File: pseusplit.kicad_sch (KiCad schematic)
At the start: 146 parts, among them J1 USB_C_Receptacle_USB2.0_14P, J3 ST7789 320x240, Q1 DTC123J, SW1 Reset_SW, U1 IS31FL3733-QF, U2 XC6206PxxxMR, U4 STM32G0B1CBTx, U5 SRV05-4

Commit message: Update some part numbers, remove unnecessary MPN symbol field, dos2unix CSV files
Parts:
- C1, C2, C4, C6: MPN C13967 -> (none)
- C10, C11: MPN C28323 -> (none)
- C12, C9: MPN C1744 -> (none)
- C13: MPN C15850 -> (none)
- C14, C16: MPN C28233 -> (none)
- C17, C18: MPN C1779 -> (none)
- C3, C5, C7: MPN C49678 -> (none)
- C8: MPN C45783 -> (none)
- D1, D10, D11, D12, D13, D14, D15, D16, D17, D18, D19, D2, D20, D21, D22, D23, D24, D25, D26, D27, D28, D29, D3, D30, D31, D32, D33, D34, D37, D38, D39, D4, D5, D6, D7, D8, D9: MPN C81598 -> (none)
- D40: MPN C2297 -> (none)
- F1: MPN C2830238 -> (none)
- J1: MPN C165948 -> (none)
- LED1, LED10, LED11, LED12, LED13, LED14, LED15, LED16, LED17, LED18, LED19, LED2, LED20, LED21, LED22, LED23, LED24, LED25, LED26, LED27, LED28, LED29, LED3, LED30, LED31, LED32, LED33, LED34, LED35, LED36, LED4, LED5, LED6, LED7, LED8, LED9: MPN C183826 -> (none)
- Q1: MPN C20616358 -> (none)
- R1: MPN C4328 -> (none)
- R11, R2: MPN C149504 -> (none)
- R12, R7, R8: MPN C27834 -> (none)
- R3: MPN C17414 -> (none)
- R4, R5: MPN C17604 -> (none)
- R6: MPN C17514 -> (none)
- SW1: MPN C318884 -> (none)
- U1: MPN C506251 -> (none)
- U2: MPN C5446 -> (none)
- U4: MPN C2847904 -> (none)
- U5: MPN C558418 -> (none)

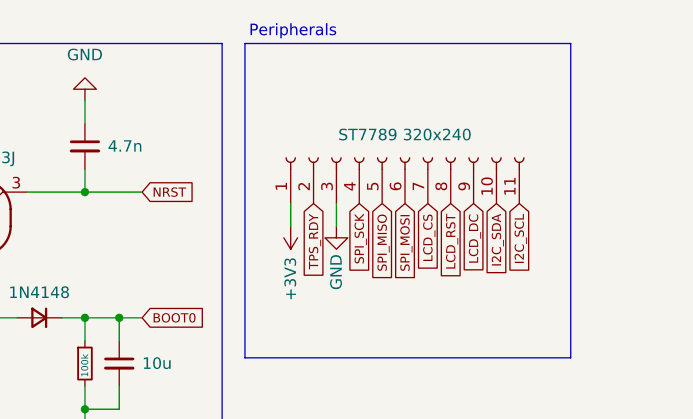
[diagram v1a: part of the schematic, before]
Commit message: Update tantalum capacitor footprint & part, remove LEDs from BOM & provide link
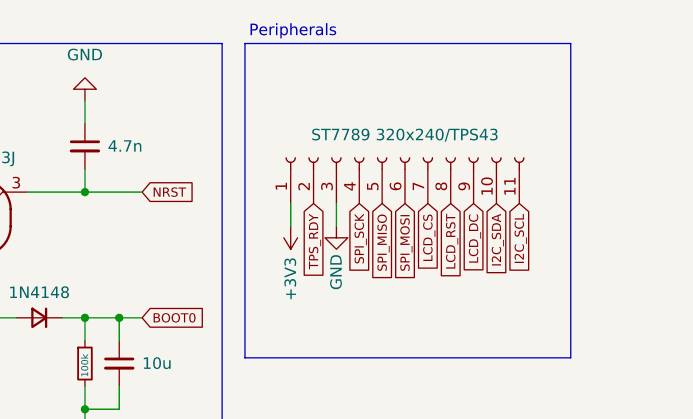
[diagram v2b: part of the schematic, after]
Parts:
- C8: footprint Capacitor_SMD:C_0805_2012Metric -> Capacitor_Tantalum_SMD:CP_EIA-3216-18_Kemet-A
- J3: value ST7789 320x240 -> ST7789 320x240/TPS43
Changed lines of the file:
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@@
 	(title_block
 		(title "pseusplit keyboard")
-		(date "2025-06-08")
+		(date "2025-06-25")
 		(rev "0.1.0")
 		(company "jack@pngu.org")
@@
 			)
 		)
-		(property "Footprint" "Capacitor_SMD:C_0805_2012Metric"
+		(property "Footprint" "Capacitor_Tantalum_SMD:CP_EIA-3216-18_Kemet-A"
 			(at 246.38 111.76 0)
 			(effects
@@
 			)
 		)
-		(property "Value" "ST7789 320x240"
+		(property "Value" "ST7789 320x240/TPS43"
 			(at 347.98 26.67 90)
 			(effects
